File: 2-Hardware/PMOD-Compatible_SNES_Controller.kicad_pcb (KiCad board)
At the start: 2 copper layers, 64.8 x 20.3 mm, 5 parts, among them J1 PMOD_SINGLE, P1 CONN_1x7

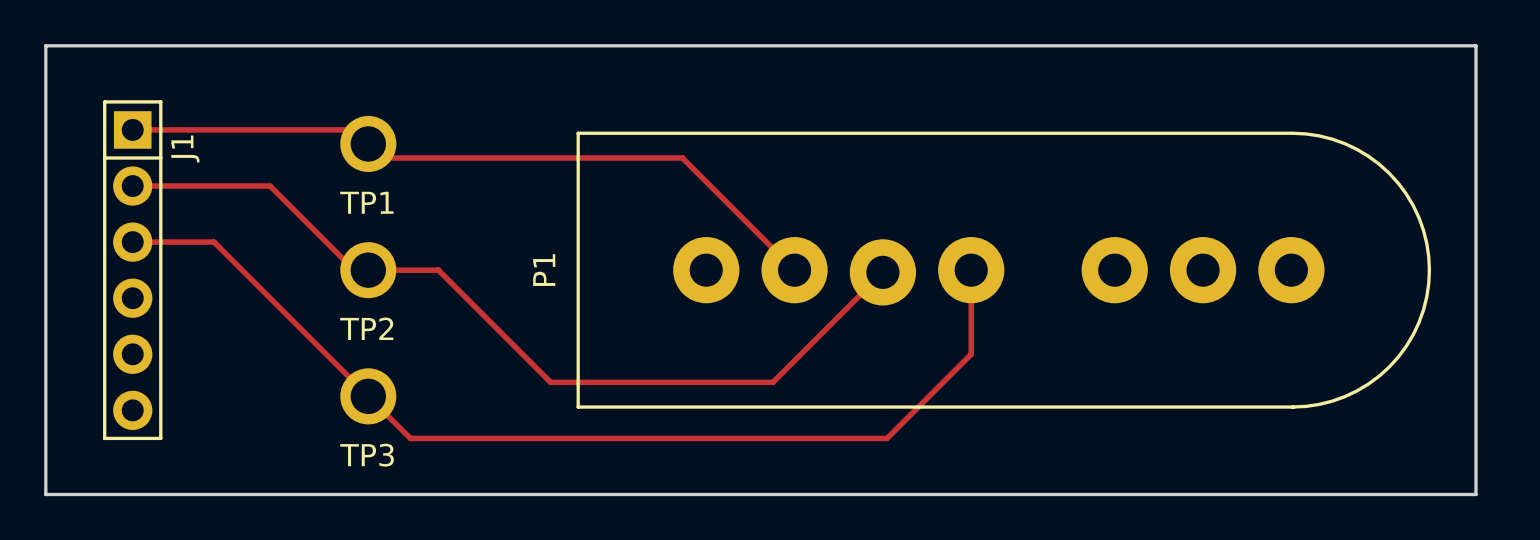
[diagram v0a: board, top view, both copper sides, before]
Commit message: Rev'ed the board and added testpoint
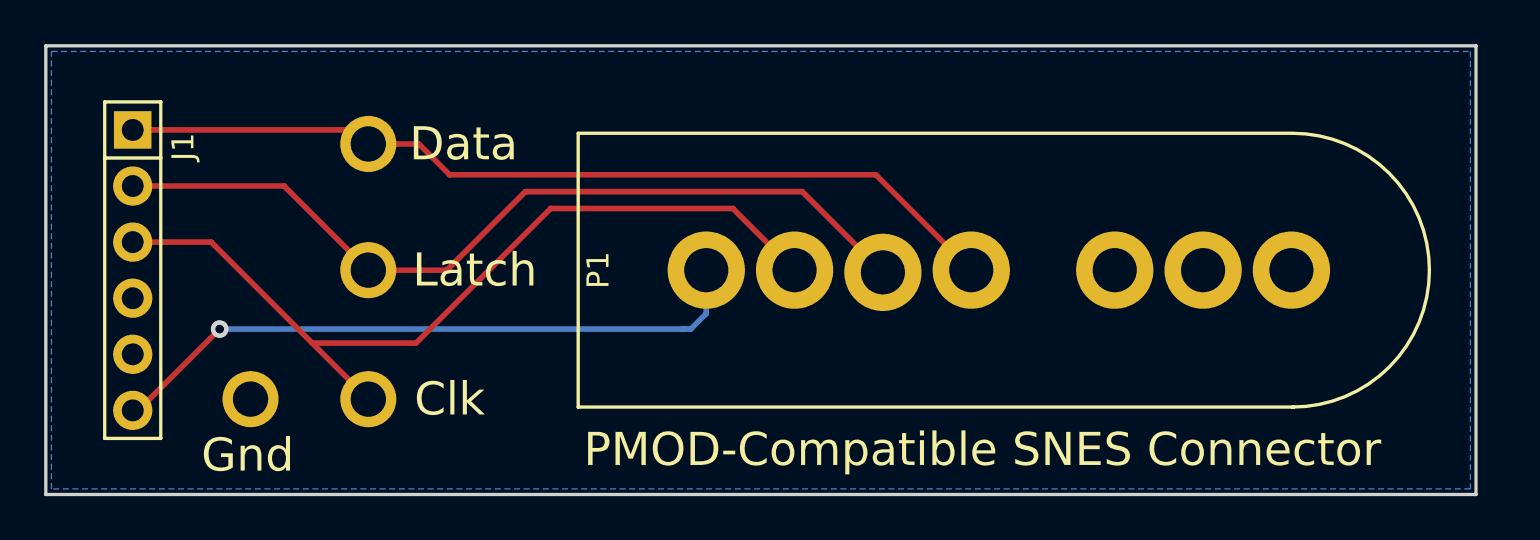
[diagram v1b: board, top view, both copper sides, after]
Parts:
- added TP4: TEST_POINT, Connectors:TESTPOINT_063, F.Cu at (90.6, 102.4)
- moved TP3 0.13 mm to (95.9, 102.4)
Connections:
- net Net-(J1-Pad5) renamed GND
- P1 pad 2: Net-(J1-Pad1) -> Net-(J1-Pad3)
- P1 pad 4: Net-(J1-Pad3) -> Net-(J1-Pad1)
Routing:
- net Net-(J1-Pad6): track 0.00 -> 29.9 mm, vias 0 -> 1
- net Net-(J1-Pad1): track 32.6 -> 40.6 mm
- net Net-(J1-Pad3): track 47.0 -> 39.3 mm
- net Net-(J1-Pad2): track 39.7 -> 38.5 mm
- added copper zone on B.Cu, net GND
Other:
- net class Default: trace_width 0.25 -> 0.254
- board text added: "Clk"
- board text added: "Data"
- board text added: "Gnd"
- board text added: "Latch"
- board text added: "PMOD-Compatible SNES Connector"
